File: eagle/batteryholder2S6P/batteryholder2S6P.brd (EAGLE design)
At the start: 185.4 x 89.7 mm, 10 parts, among them J3 POWER_JACKPTH_BREAD

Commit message: new PCB files (batteryholder, templog2, ...)
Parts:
- removed BT4: KEYSTONE_1048KEYSTONE_1048_0_0, Keystone - 1048:KEYSTONE_1048_0
- added BT5, BT6, BT7: KEYSTONE_1048KEYSTONE_1048_0_0, Keystone - 1048:KEYSTONE_1048_0
- moved J3 41.7 mm to (147.5, 57.0)
- moved J1 41.6 mm to (140.0, 31.0)
- moved H3 41.3 mm to (139.0, 85.0)
- moved H4 41.3 mm to (139.0, 5.00)
- moved BT1 0.73 mm to (30.0, 45.0)
- moved BT3 0.60 mm to (112.0, 45.0)
- moved BT2 0.56 mm to (71.0, 45.0)
- moved H1 0.43 mm to (5.00, 85.0)
- moved H2 0.11 mm to (5.00, 5.00)
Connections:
- net BOTTOM_MINUS: now also BT5.1, BT5.3, BT6.1, BT6.3, BT7.1, BT7.3; no longer BT1.2, BT1.4, BT2.2, BT2.4
- net TOP_MINUS: now also BT5.2, BT5.4, BT6.2, BT6.4, BT7.2, BT7.4; no longer BT4.1, BT4.3
- net TOP_PLUS: now also BT1.2, BT1.4, BT2.2, BT2.4; no longer BT4.2, BT4.4
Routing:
- net BOTTOM_MINUS: track 32.3 -> 41.0 mm, vias 20 -> 0
- net TOP_PLUS: track 17.9 -> 21.2 mm
- net TOP_MINUS: track 51.4 -> 49.7 mm, vias 35 -> 31
- removed copper zone on layer 1, net BOTTOM_MINUS
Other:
- board size 185.4 x 89.7 mm -> 144 x 90 mm
- board text added: "2S6P"
- board text removed: "2S4P"

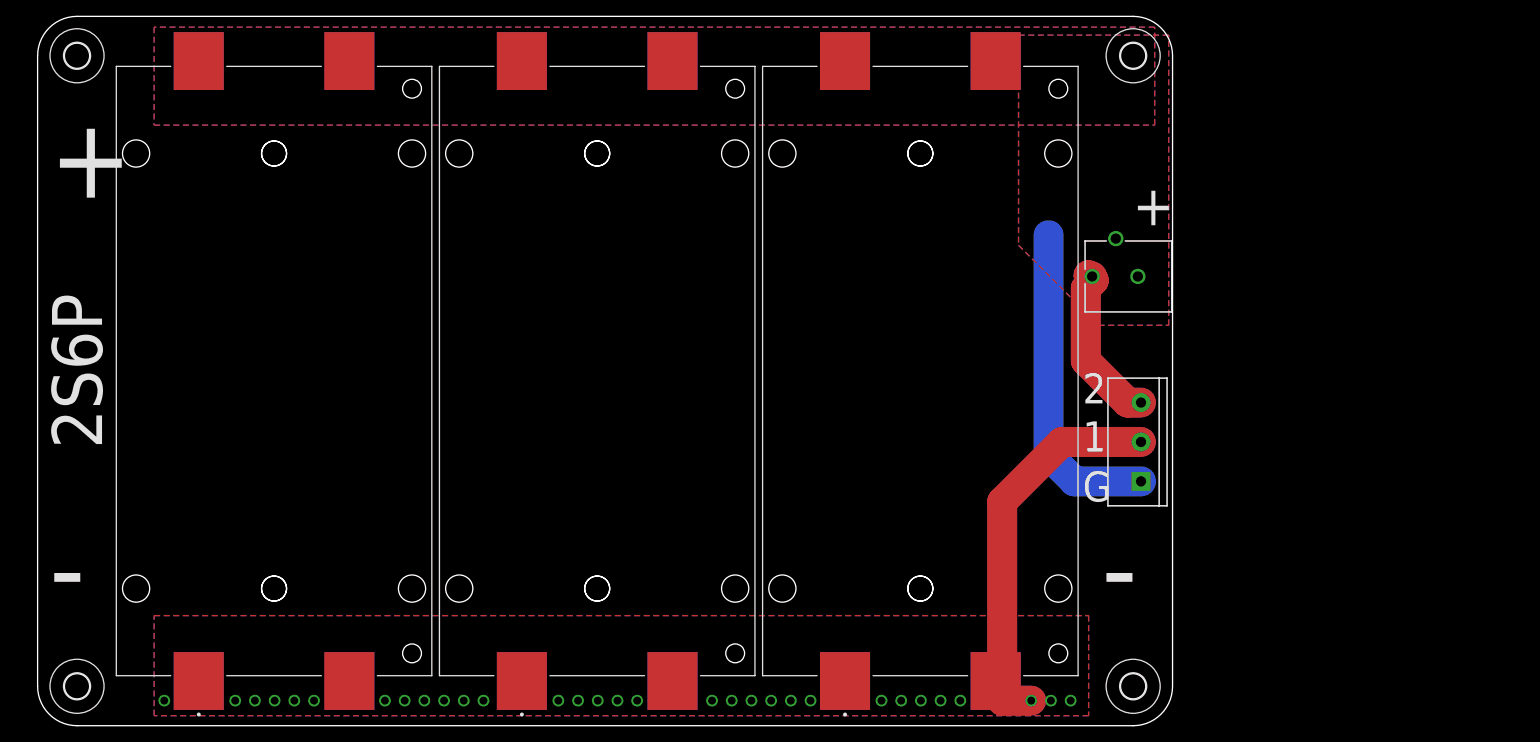
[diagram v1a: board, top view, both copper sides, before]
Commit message: batteryholder 2S6P added polarity signs on silkscreen
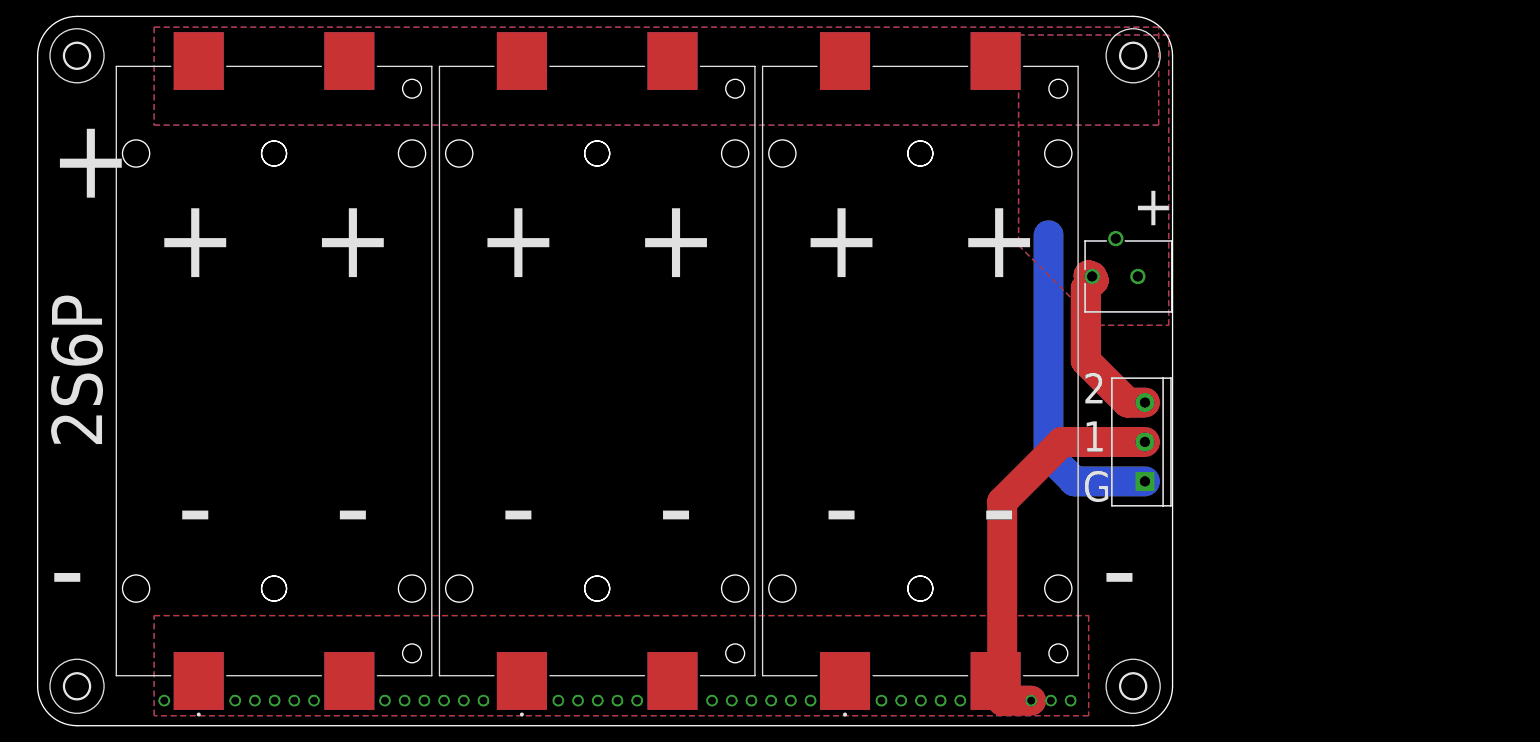
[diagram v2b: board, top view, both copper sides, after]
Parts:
- moved J1 0.50 mm to (140.5, 31.0)
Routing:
- net TOP_PLUS: track 21.2 -> 21.7 mm
- net TOP_MINUS: track 49.7 -> 50.2 mm
- net BOTTOM_MINUS: track 41.0 -> 41.5 mm
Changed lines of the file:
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@@
 <text x="132.588" y="28.448" size="3.81" layer="21" ratio="15">G</text>
 <text x="5" y="45" size="6.35" layer="21" ratio="10" rot="R90" align="center">2S6P</text>
+<text x="20" y="62" size="10.16" layer="21" ratio="15" align="center">+</text>
+<text x="40" y="62" size="10.16" layer="21" ratio="15" align="center">+</text>
+<text x="61" y="62" size="10.16" layer="21" ratio="15" align="center">+</text>
+<text x="81" y="62" size="10.16" layer="21" ratio="15" align="center">+</text>
+<text x="102" y="62" size="10.16" layer="21" ratio="15" align="center">+</text>
+<text x="122" y="62" size="10.16" layer="21" ratio="15" align="center">+</text>
+<text x="20" y="28" size="10.16" layer="21" ratio="15" align="center">-</text>
+<text x="40" y="28" size="10.16" layer="21" ratio="15" align="center">-</text>
+<text x="61" y="28" size="10.16" layer="21" ratio="15" align="center">-</text>
+<text x="81" y="28" size="10.16" layer="21" ratio="15" align="center">-</text>
+<text x="102" y="28" size="10.16" layer="21" ratio="15" align="center">-</text>
+<text x="122" y="28" size="10.16" layer="21" ratio="15" align="center">-</text>
+<text x="20" y="62" size="10.16" layer="22" ratio="15" rot="MR0" align="center">-</text>
+<text x="40" y="62" size="10.16" layer="22" ratio="15" rot="MR0" align="center">-</text>
+<text x="61" y="62" size="10.16" layer="22" ratio="15" rot="MR0" align="center">-</text>
+<text x="81" y="62" size="10.16" layer="22" ratio="15" rot="MR0" align="center">-</text>
+<text x="102" y="62" size="10.16" layer="22" ratio="15" rot="MR0" align="center">-</text>
+<text x="122" y="62" size="10.16" layer="22" ratio="15" rot="MR0" align="center">-</text>
+<text x="20" y="28" size="10.16" layer="22" ratio="15" rot="MR0" align="center">+</text>
+<text x="40" y="28" size="10.16" layer="22" ratio="15" rot="MR0" align="center">+</text>
+<text x="61" y="28" size="10.16" layer="22" ratio="15" rot="MR0" align="center">+</text>
+<text x="81" y="28" size="10.16" layer="22" ratio="15" rot="MR0" align="center">+</text>
+<text x="102" y="28" size="10.16" layer="22" ratio="15" rot="MR0" align="center">+</text>
+<text x="122" y="28" size="10.16" layer="22" ratio="15" rot="MR0" align="center">+</text>
 </plain>
 <attributes>
@@
 <attribute name="POPULARITY" value="7" x="139" y="5" size="1.778" layer="27" display="off"/>
 </element>
-<element name="J1" library="SparkFun-Connectors" library_urn="urn:adsk.eagle:library:513" package="SCREWTERMINAL-5MM-3" package3d_urn="urn:adsk.eagle:package:38070/1" value="" x="140" y="31" smashed="yes" rot="R90">
-<attribute name="PROD_ID" value="CONN-10134" x="140" y="31" size="1.778" layer="27" rot="R90" display="off"/>
-<attribute name="SF_SKU" value="PRT-08433" x="140" y="31" size="1.778" layer="27" rot="R90" display="off"/>
-<attribute name="VALUE" x="138.095" y="34.429" size="0.6096" layer="27" font="vector" ratio="20" rot="R90"/>
+<element name="J1" library="SparkFun-Connectors" library_urn="urn:adsk.eagle:library:513" package="SCREWTERMINAL-5MM-3" package3d_urn="urn:adsk.eagle:package:38070/1" value="" x="140.5" y="31" smashed="yes" rot="R90">
+<attribute name="PROD_ID" value="CONN-10134" x="140.5" y="31" size="1.778" layer="27" rot="R90" display="off"/>
+<attribute name="SF_SKU" value="PRT-08433" x="140.5" y="31" size="1.778" layer="27" rot="R90" display="off"/>
+<attribute name="VALUE" x="138.595" y="34.429" size="0.6096" layer="27" font="vector" ratio="20" rot="R90"/>
 </element>
 <element name="BT5" library="Keystone - 1048" package="KEYSTONE_1048_0" value="KEYSTONE_1048KEYSTONE_1048_0_0" x="30" y="45" smashed="yes" rot="MR270">
@@
 <via x="131.07" y="3.184" extent="1-16" drill="1"/>
 <wire x1="122.38" y1="28.4" x2="129.98" y2="36" width="3.81" layer="1"/>
-<wire x1="129.98" y1="36" x2="140" y2="36" width="3.81" layer="1"/>
+<wire x1="129.98" y1="36" x2="140.5" y2="36" width="3.81" layer="1"/>
 <via x="128.57" y="3.184" extent="1-16" drill="1"/>
 <via x="126.07" y="3.184" extent="1-16" drill="1"/>
@@
 <vertex x="14.78" y="88.63"/>
 <vertex x="14.78" y="76.2"/>
-<vertex x="141.732" y="76.2"/>
-<vertex x="141.732" y="88.63"/>
+<vertex x="142.232" y="76.2"/>
+<vertex x="142.232" y="88.63"/>
 </polygon>
 <contactref element="BT3" pad="4"/>
@@
 </polygon>
 <wire x1="133.35" y1="57.15" x2="133.8" y2="57" width="3.81" layer="1"/>
-<wire x1="140" y1="41" x2="138.3" y2="41" width="3.81" layer="1"/>
+<wire x1="140.5" y1="41" x2="138.3" y2="41" width="3.81" layer="1"/>
 <wire x1="138.3" y1="41" x2="133" y2="46.3" width="3.81" layer="1"/>
 <wire x1="133" y1="46.3" x2="133" y2="55.5" width="3.81" layer="1"/>
@@
 <vertex x="14.78" y="88.63"/>
 <vertex x="14.78" y="76.2"/>
-<vertex x="141.732" y="76.2"/>
-<vertex x="141.732" y="88.63"/>
+<vertex x="142.232" y="76.2"/>
+<vertex x="142.232" y="88.63"/>
 </polygon>
 <contactref element="J1" pad="1"/>
@@
 </polygon>
 <wire x1="128.27" y1="34.29" x2="128.27" y2="62.23" width="3.81" layer="16"/>
-<wire x1="140" y1="31" x2="131.56" y2="31" width="3.81" layer="16"/>
+<wire x1="140.5" y1="31" x2="131.56" y2="31" width="3.81" layer="16"/>
 <wire x1="131.56" y1="31" x2="128.27" y2="34.29" width="3.81" layer="16"/>
 </signal>

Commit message: additional eagle boards
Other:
- outline, holes or cut-outs redrawn
- board text added: "rev. B"
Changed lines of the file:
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@@
 <wire x1="139" y1="90" x2="5" y2="90" width="0.1524" layer="20"/>
 <wire x1="5" y1="90" x2="0" y2="85" width="0.1524" layer="20" curve="90"/>
-<wire x1="0" y1="85" x2="0" y2="5" width="0.1524" layer="20"/>
 <wire x1="0" y1="5" x2="5" y2="0" width="0.1524" layer="20" curve="90"/>
 <wire x1="5" y1="0" x2="139" y2="0" width="0.1524" layer="20"/>
@@
 <wire x1="144" y1="5" x2="144" y2="85" width="0.1524" layer="20"/>
 <wire x1="144" y1="85" x2="139" y2="90" width="0.1524" layer="20" curve="90"/>
-<text x="1.5" y="67" size="10.16" layer="21" ratio="15">+</text>
-<text x="1.5" y="15" size="10.16" layer="21" ratio="15">-</text>
-<text x="135" y="15" size="10.16" layer="21" ratio="15">-</text>
-<text x="138.938" y="63.5" size="5.08" layer="21" ratio="15">+</text>
-<text x="8.75" y="15" size="10.16" layer="22" ratio="15" rot="MR0">+</text>
-<text x="8.5" y="67" size="10.16" layer="22" ratio="15" rot="MR0">-</text>
-<text x="142.494" y="63.5" size="5.08" layer="22" ratio="15" rot="MR0">-</text>
-<text x="142.25" y="15" size="10.16" layer="22" ratio="15" rot="MR0">+</text>
-<polygon width="0.254" layer="29">
-<vertex x="134.35" y="68.58"/>
-<vertex x="141.97" y="68.58"/>
-<vertex x="141.97" y="76.2"/>
-<vertex x="134.35" y="76.2"/>
-</polygon>
-<polygon width="0.254" layer="30">
-<vertex x="134.35" y="68.58"/>
-<vertex x="141.97" y="68.58"/>
-<vertex x="141.97" y="76.2"/>
-<vertex x="134.35" y="76.2"/>
-</polygon>
+<text x="5" y="62" size="10.16" layer="21" ratio="15" align="center">+</text>
+<text x="5" y="28" size="10.16" layer="21" ratio="15" align="center">-</text>
+<text x="5" y="28" size="10.16" layer="22" ratio="15" rot="MR0" align="center">+</text>
+<text x="5" y="62" size="10.16" layer="22" ratio="15" rot="MR0" align="center">-</text>
 <text x="132.588" y="40.894" size="3.81" layer="21" ratio="15">2</text>
 <text x="132.588" y="34.798" size="3.81" layer="21" ratio="15">1</text>
@@
 <text x="102" y="28" size="10.16" layer="22" ratio="15" rot="MR0" align="center">+</text>
 <text x="122" y="28" size="10.16" layer="22" ratio="15" rot="MR0" align="center">+</text>
+<wire x1="0" y1="5" x2="0" y2="76.1" width="0.1524" layer="20"/>
+<wire x1="0" y1="76" x2="0" y2="85" width="0.1524" layer="20"/>
+<text x="20.2" y="43.5" size="2" layer="21" ratio="10" align="center">rev. B</text>
+<text x="20.2" y="46.5" size="2" layer="21" ratio="10" align="center">2S6P</text>
+<circle x="5" y="18" radius="3.5" width="0.1524" layer="20"/>
+<circle x="5" y="72" radius="3.5" width="0.1524" layer="20"/>
+<circle x="139" y="72" radius="3.5" width="0.1524" layer="20"/>
+<circle x="139" y="18" radius="3.5" width="0.1524" layer="20"/>
 </plain>
 <attributes>
@@
 <polygon width="0.254" layer="1" thermals="no">
 <vertex x="14.78" y="1.27"/>
-<vertex x="14.78" y="13.97"/>
-<vertex x="133.35" y="13.97"/>
+<vertex x="14.78" y="21.47"/>
+<vertex x="133.35" y="21.47"/>
 <vertex x="133.35" y="1.27"/>
 </polygon>
@@
 <polygon width="0.254" layer="16" thermals="no">
 <vertex x="14.78" y="1.27"/>
-<vertex x="14.78" y="13.97"/>
-<vertex x="133.35" y="13.97"/>
+<vertex x="14.78" y="21.47"/>
+<vertex x="133.35" y="21.47"/>
 <vertex x="133.35" y="1.27"/>
 </polygon>
@@
 <polygon width="0.254" layer="1" thermals="no">
 <vertex x="14.78" y="88.63"/>
-<vertex x="14.78" y="76.2"/>
-<vertex x="142.232" y="76.2"/>
+<vertex x="14.78" y="68.2"/>
+<vertex x="142.232" y="68.2"/>
 <vertex x="142.232" y="88.63"/>
 </polygon>
@@
 <polygon width="0.254" layer="16" thermals="no">
 <vertex x="14.78" y="88.63"/>
-<vertex x="14.78" y="76.2"/>
-<vertex x="142.232" y="76.2"/>
+<vertex x="14.78" y="68.2"/>
+<vertex x="142.232" y="68.2"/>
 <vertex x="142.232" y="88.63"/>
 </polygon>
 <contactref element="J1" pad="1"/>
 <contactref element="J3" pad="GND"/>
-<polygon width="0.1524" layer="16" isolate="1.524">
+<polygon width="0.1524" layer="16" isolate="1.524" thermals="no">
 <vertex x="124.46" y="87.63"/>
 <vertex x="124.46" y="60.96"/>
